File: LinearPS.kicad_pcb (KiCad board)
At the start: 2 copper layers, 100 x 100 mm, 84 parts, among them J1 Conn_01x03, J2 Conn_01x02, J3 Conn_01x03, J4 Conn_01x01, J5 Conn_01x01, J6 Conn_01x01, J7 Conn_01x01, J8 Conn_01x02, Q1 2N2222, Q2 TIP41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

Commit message: Added outputs for voltage and current meters
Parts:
- removed R28, R29: 10k, Resistors_THT:R_Axial_DIN0207_L6.3mm_D2.5mm_P7.62mm_Horizontal
- removed U3: LM7805_TO220, TO_SOT_Packages_THT:TO-220-3_Vertical
- added D22: 1N4733A, Diodes_THT:D_DO-41_SOD81_P7.62mm_Horizontal, F.Cu at (110.6, 53.4)
- added J9: Conn_01x02, Pin_Headers:Pin_Header_Straight_1x02_Pitch2.54mm, F.Cu at (104.7, 100.4)
- added R32: 1k, Resistors_THT:R_Axial_DIN0411_L9.9mm_D3.6mm_P12.70mm_Horizontal, F.Cu at (106.8, 65.8)
- added RV3: 10k, Potentiometers:Potentiometer_Trimmer_Bourns_3296W, F.Cu at (104.2, 95.7)
- added RV4: 10k, Potentiometers:Potentiometer_Trimmer_Bourns_3296W, F.Cu at (128.0, 100.2)
- added RV5: 10k, Potentiometers:Potentiometer_Trimmer_Bourns_3296W, F.Cu at (133.8, 97.9)
- moved J8 16.2 mm to (118.6, 64.5)
- moved R16 7.12 mm to (123.7, 110.0)
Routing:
- net Net-(D8-Pad1): track 80.8 -> 101.5 mm
- net Net-(C12-Pad1): track 17.6 -> 35.2 mm
- net Net-(C4-Pad1): track 156.4 -> 173.0 mm
- net GND: track 362.9 -> 353.0 mm
- net Net-(J3-Pad2): track 8.53 -> 17.9 mm
- net Net-(Q1-Pad2): track 45.1 -> 53.6 mm
- net Net-(R5-Pad1): track 7.37 -> 13.1 mm
- net Net-(Q2-Pad3): track 159.1 -> 153.8 mm
- net Net-(C1-Pad1): track 473.4 -> 477.4 mm
- net Net-(J3-Pad1): track 7.79 -> 10.5 mm
- net Net-(C6-Pad1): track 162.6 -> 164.3 mm
- net Net-(R23-Pad1): track 26.2 -> 27.1 mm
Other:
- board text removed: "LM7805"

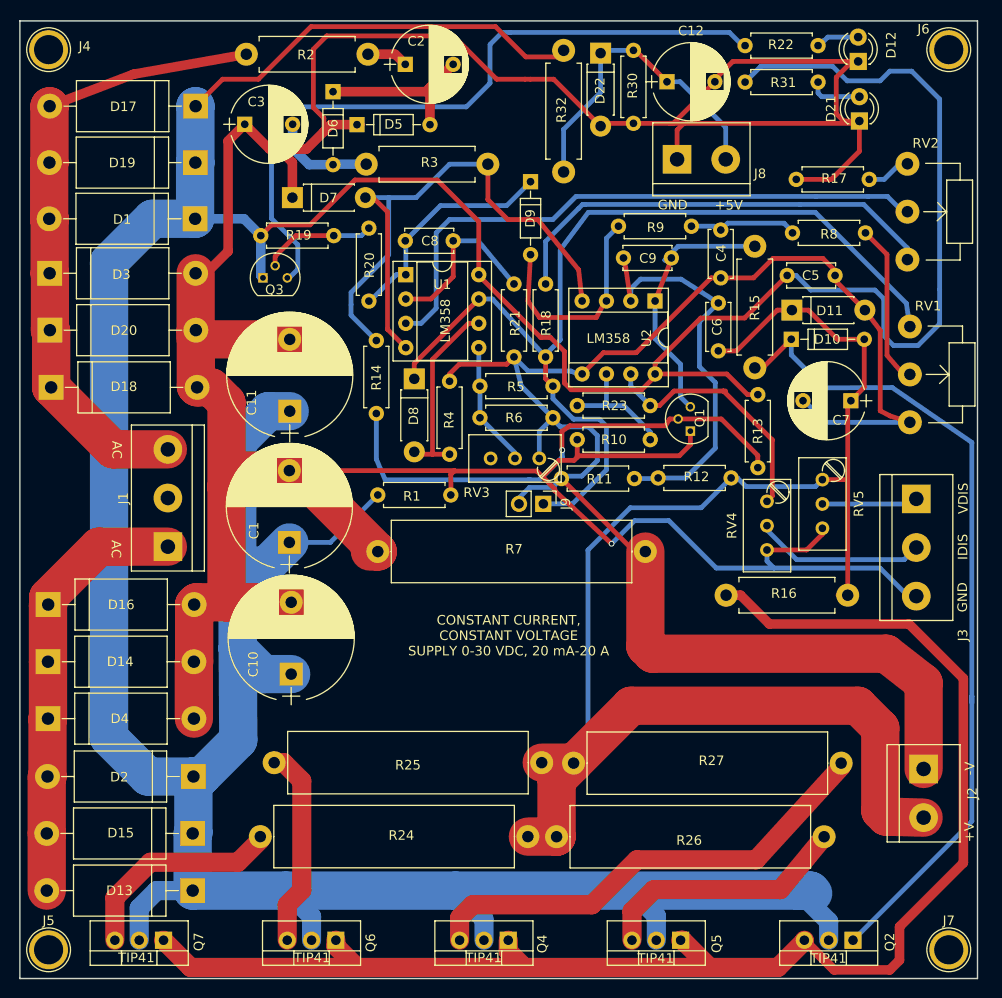
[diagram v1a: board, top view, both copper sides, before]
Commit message: Added better TO-220 mounting
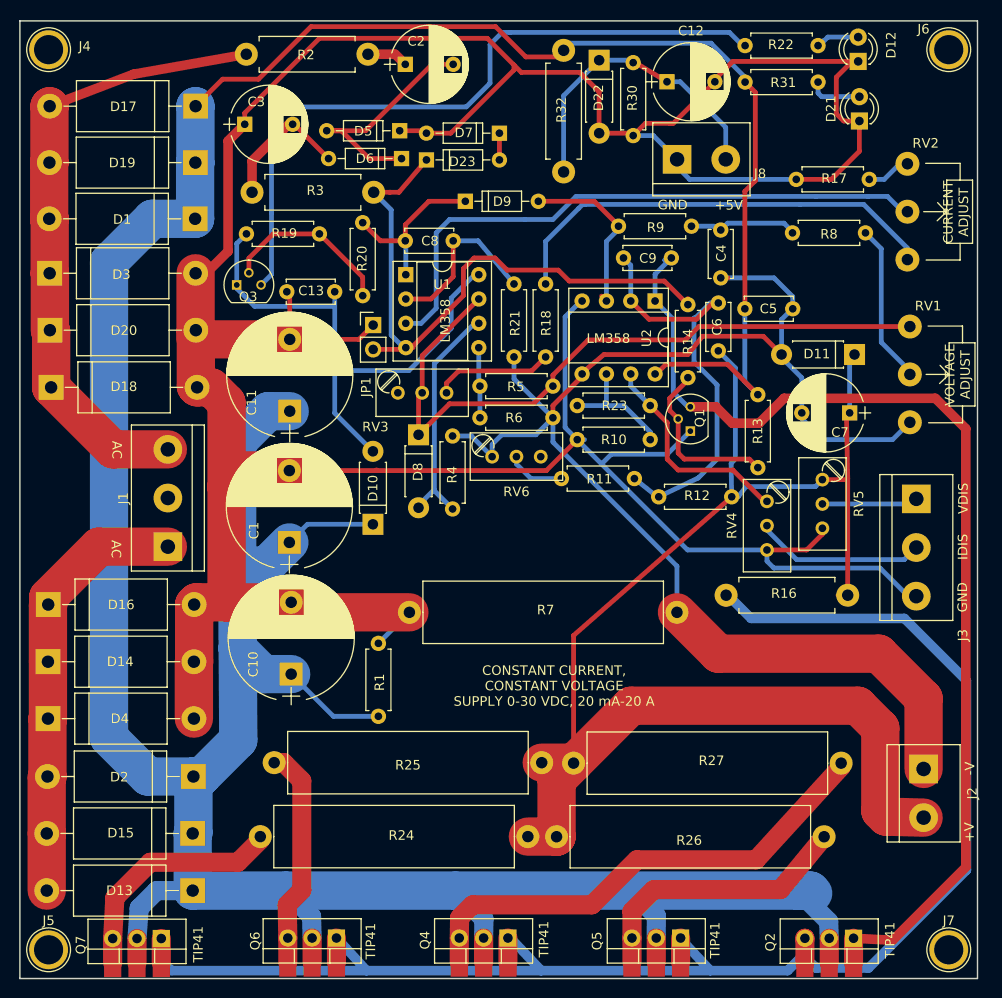
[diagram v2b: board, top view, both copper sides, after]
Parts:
- removed J9: Conn_01x02, Pin_Headers:Pin_Header_Straight_1x02_Pitch2.54mm
- removed R15: 1k, Resistors_THT:R_Axial_DIN0411_L9.9mm_D3.6mm_P12.70mm_Horizontal
- added C13: 100 nF, Capacitors_THT:C_Disc_D5.0mm_W2.5mm_P5.00mm, F.Cu at (77.9, 78.3)
- added D23: 1N4148, Diodes_THT:D_DO-35_SOD27_P7.62mm_Horizontal, F.Cu at (92.5, 64.5)
- added JP1: Jumper_NO_Small, Pin_Headers:Pin_Header_Straight_1x02_Pitch2.54mm, F.Cu at (86.9, 81.8)
- added RV6: 20k, Potentiometers:Potentiometer_Trimmer_Bourns_3296W, F.Cu at (99.3, 95.5)
- D10: value 1N4148 -> 1N4740A; footprint Diodes_THT:D_DO-35_SOD27_P7.62mm_Horizontal -> Diodes_THT:D_DO-41_SOD81_P7.62mm_Horizontal
- D7: value 1N5339B -> 1N4148; footprint Diodes_THT:D_DO-41_SOD81_P7.62mm_Horizontal -> Diodes_THT:D_DO-35_SOD27_P7.62mm_Horizontal
- Q2, Q4, Q5, Q6, Q7: footprint TO_SOT_Packages_THT:TO-220-3_Vertical -> linearps:TO-220-3_Vertical_WithPads
- R13: value 56k -> 22k
- R14: value 1k5 -> 1k
- R18: value 56k -> 33k
- RV3: value 10k -> 100k
- moved D10 47.8 mm to (86.9, 102.6), turned to 90 degrees
- moved R14 32.8 mm to (119.8, 79.6)
- moved R1 23.1 mm to (87.4, 122.6), turned to 90 degrees
- moved D7 22.6 mm to (100.1, 61.7), turned to 180 degrees
- moved RV3 16.3 mm to (89.5, 88.8), turned to 180 degrees
- moved R3 12.3 mm to (86.9, 67.9)
- moved D6 10.00 mm to (89.9, 64.4), turned to 180 degrees
- moved D11 8.02 mm to (137.2, 84.8), turned to 180 degrees
- moved R7 7.16 mm to (90.7, 111.8)
- moved D9 7.11 mm to (96.5, 68.8), turned to 0 degrees
- moved R20 7.08 mm to (85.8, 78.7), turned to 90 degrees
- moved D8 5.86 mm to (91.6, 93.2)
- moved R4 5.72 mm to (95.2, 101.0)
- moved C5 5.63 mm to (130.7, 80.1)
- moved D5 4.50 mm to (89.7, 61.5), turned to 180 degrees
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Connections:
- D10 pad 1: Net-(D10-Pad1) -> Net-(C1-Pad1)
- D10 pad 2: Net-(C6-Pad1) -> Net-(C13-Pad2)
- D7 pad 1: GND -> Net-(D23-Pad2)
- D7 pad 2: Net-(D7-Pad2) -> GND
- Q2 pad 1: Net-(D10-Pad1) -> Net-(C9-Pad1)
- Q3 pad 1: Net-(C1-Pad1) -> Net-(C13-Pad2)
- R11 pad 1: Net-(C4-Pad1) -> Net-(R11-Pad1)
- R14 pad 1: Net-(D7-Pad2) -> Net-(D23-Pad1)
- R18 pad 1: Net-(D8-Pad1) -> Net-(R18-Pad1)
- R19 pad 1: Net-(C1-Pad1) -> Net-(C13-Pad2)
- R3 pad 1: Net-(D7-Pad2) -> Net-(D23-Pad1)
- RV3 pad 1: Net-(C4-Pad1) -> (no net)
- RV3 pad 2: Net-(R5-Pad1) -> Net-(D8-Pad1)
- RV3 pad 3: (no net) -> Net-(R18-Pad1)
- U1 pad 4: Net-(D7-Pad2) -> Net-(D23-Pad1)
- U1 pad 8: Net-(C1-Pad1) -> Net-(C13-Pad2)
- U2 pad 4: Net-(D7-Pad2) -> GND
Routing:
- net Net-(C9-Pad1): track 28.6 -> 115.7 mm
- net Net-(D10-Pad1): track 86.6 -> 0.00 mm
- net Net-(C1-Pad1): track 477.4 -> 395.8 mm
- net Net-(D7-Pad2): track 70.0 -> 0.00 mm
- net Net-(D23-Pad1): track 0.00 -> 68.0 mm
- net Net-(C13-Pad2): track 0.00 -> 57.3 mm
- net Net-(Q1-Pad2): track 53.6 -> 18.0 mm, vias 1 -> 0
- net Net-(D8-Pad1): track 101.5 -> 74.2 mm
- net Net-(C4-Pad1): track 173.0 -> 152.4 mm
- net GND: track 353.0 -> 373.5 mm, vias 1 -> 0
- net Net-(Q2-Pad3): track 153.8 -> 172.0 mm
- net Net-(R18-Pad1): track 0.00 -> 12.8 mm
- net Net-(C6-Pad1): track 164.3 -> 155.4 mm
- net Net-(C2-Pad2): track 17.6 -> 25.1 mm
- net Net-(C8-Pad2): track 24.5 -> 17.9 mm
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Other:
- board text added: "CURRENT ADJUST"
- board text added: "VOLTAGE ADJUST"

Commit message: Change the voltage and current sense output
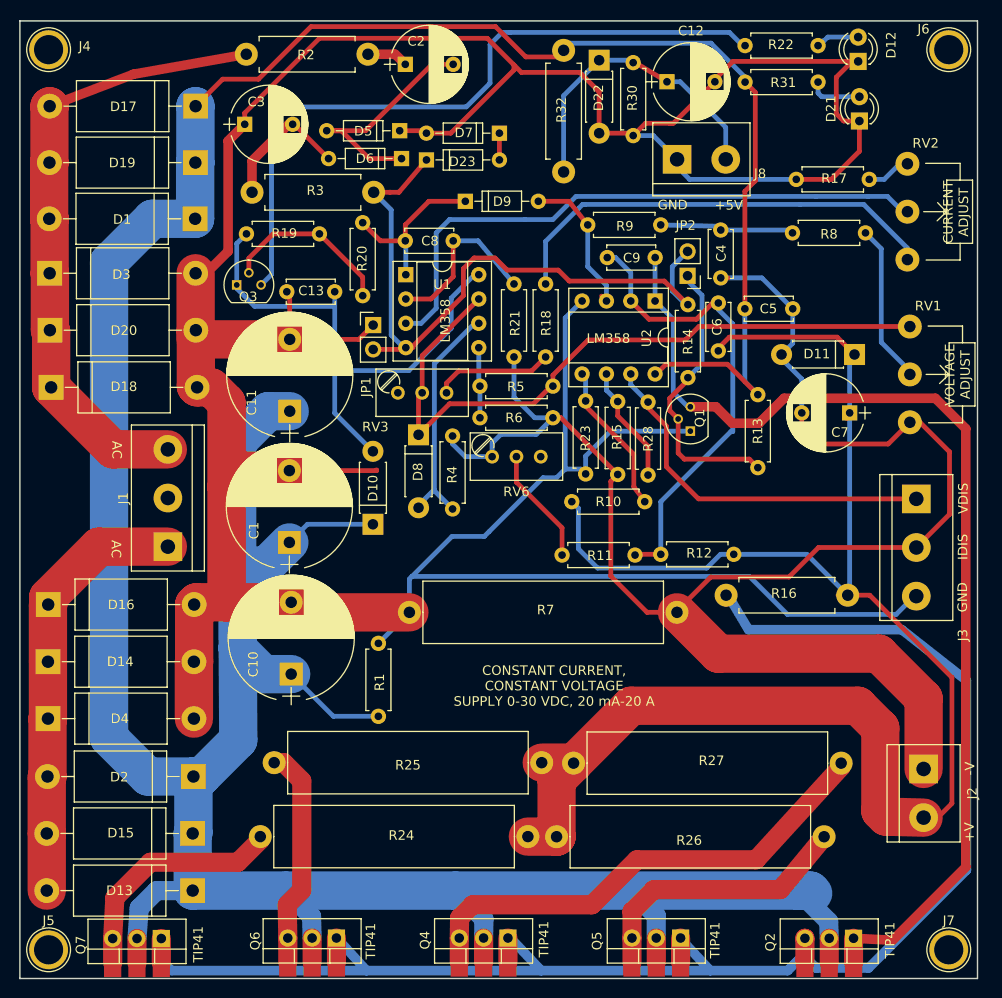
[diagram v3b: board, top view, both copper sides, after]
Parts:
- removed RV4, RV5: 10k, Potentiometers:Potentiometer_Trimmer_Bourns_3296W
- added JP2: Jumper_NO_Small, Pin_Headers:Pin_Header_Straight_1x02_Pitch2.54mm, F.Cu at (119.7, 76.6)
- added R15: 10k, Resistors_THT:R_Axial_DIN0207_L6.3mm_D2.5mm_P7.62mm_Horizontal, F.Cu at (112.4, 89.7)
- added R28: 10k, Resistors_THT:R_Axial_DIN0207_L6.3mm_D2.5mm_P7.62mm_Horizontal, F.Cu at (115.6, 89.8)
- R10: value 10k -> 100k
- moved R23 9.82 mm to (109.1, 97.3), turned to 90 degrees
- moved R11 7.99 mm to (106.6, 105.8)
- moved R10 6.50 mm to (107.6, 100.2)
- moved R12 6.01 mm to (124.5, 105.7)
- moved R9 3.21 mm to (109.3, 71.3)
- moved C9 1.69 mm to (116.3, 74.7)
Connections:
- J3 pad 2: Net-(J3-Pad2) -> Net-(C4-Pad1)
- R10 pad 1: GND -> Net-(C6-Pad1)
- R23 pad 1: Net-(R23-Pad1) -> GND
- U2 pad 5: Net-(C4-Pad1) -> Net-(R10-Pad2)
- U2 pad 6: Net-(R10-Pad2) -> Net-(R15-Pad1)
- U2 pad 7: Net-(R23-Pad1) -> Net-(J3-Pad1)
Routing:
- net Net-(J3-Pad1): track 10.5 -> 39.9 mm
- net Net-(R23-Pad1): track 23.3 -> 0.00 mm
- net Net-(C4-Pad1): track 152.4 -> 173.3 mm
- net Net-(C6-Pad1): track 155.4 -> 175.3 mm
- net Net-(J3-Pad2): track 17.9 -> 0.00 mm
- net GND: track 373.5 -> 388.7 mm
- net Net-(R15-Pad1): track 0.00 -> 12.8 mm
- net Net-(JP2-Pad1): track 18.0 -> 29.9 mm
- net Net-(D23-Pad1): track 68.0 -> 75.0 mm
- net Net-(R11-Pad1): track 6.45 -> 12.3 mm
- net Net-(C6-Pad2): track 45.0 -> 49.5 mm
- net Net-(R10-Pad2): track 13.5 -> 16.9 mm
- net Net-(C9-Pad1): track 115.7 -> 112.6 mm
- net Net-(C4-Pad2): track 11.5 -> 14.5 mm
- net Net-(D9-Pad2): track 19.1 -> 16.8 mm

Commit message: Changed voltage and current meter output
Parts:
- added JP3: Jumper_NO_Small, Pin_Headers:Pin_Header_Straight_1x02_Pitch2.54mm, F.Cu at (93.8, 105.9)
- Q1: value 2N2222 -> 2N3904
- Q3: value 2N2907 -> 2N3906
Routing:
- net GND: track 388.7 -> 370.7 mm
- net Net-(C13-Pad2): track 57.3 -> 74.4 mm
- net Net-(C1-Pad1): track 395.8 -> 404.6 mm
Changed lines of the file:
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@@
 (kicad_pcb (version 4) (host pcbnew 4.0.7)
   (general
-    (links 168)
+    (links 170)
     (no_connects 0)
     (area 49.924999 49.924999 150.075001 150.075001)
     (thickness 1.6)
     (drawings 23)
-    (tracks 608)
+    (tracks 612)
     (zones 0)
-    (modules 90)
+    (modules 91)
     (nets 42)
   )
@@
       (effects (font (size 1 1) (thickness 0.15)))
     )
-    (fp_text value 2N2222 (at 1.27 2.79 90) (layer F.Fab)
+    (fp_text value 2N3904 (at 1.27 2.79 90) (layer F.Fab)
       (effects (font (size 1 1) (thickness 0.15)))
     )
@@
       (effects (font (size 1 1) (thickness 0.15)))
     )
-    (fp_text value 2N2907 (at 1.27 2.79) (layer F.Fab)
+    (fp_text value 2N3906 (at 1.27 2.79) (layer F.Fab)
       (effects (font (size 1 1) (thickness 0.15)))
     )
@@
     )
   )
+  (module Pin_Headers:Pin_Header_Straight_1x02_Pitch2.54mm (layer F.Cu)
+    (at 93.76664 105.86466 90)
+    (descr "Through hole straight pin header, 1x02, 2.54mm pitch, single row")
+    (tags "Through hole pin header THT 1x02 2.54mm single row")
+    (fp_text reference JP3 (at 0.16764 5.588 90) (layer F.SilkS)
+      (effects (font (size 1 1) (thickness 0.15)))
+    )
+    (fp_text value Jumper_NO_Small (at 0 4.87 90) (layer F.Fab)
+      (effects (font (size 1 1) (thickness 0.15)))
+    )
+    (fp_line (start -0.635 -1.27) (end 1.27 -1.27) (layer F.Fab) (width 0.1))
+    (fp_line (start 1.27 -1.27) (end 1.27 3.81) (layer F.Fab) (width 0.1))
+    (fp_line (start 1.27 3.81) (end -1.27 3.81) (layer F.Fab) (width 0.1))
+    (fp_line (start -1.27 3.81) (end -1.27 -0.635) (layer F.Fab) (width 0.1))
+    (fp_line (start -1.27 -0.635) (end -0.635 -1.27) (layer F.Fab) (width 0.1))
+    (fp_line (start -1.33 3.87) (end 1.33 3.87) (layer F.SilkS) (width 0.12))
+    (fp_line (start -1.33 1.27) (end -1.33 3.87) (layer F.SilkS) (width 0.12))
+    (fp_line (start 1.33 1.27) (end 1.33 3.87) (layer F.SilkS) (width 0.12))
+    (fp_line (start -1.33 1.27) (end 1.33 1.27) (layer F.SilkS) (width 0.12))
+    (fp_line (start -1.33 0) (end -1.33 -1.33) (layer F.SilkS) (width 0.12))
+    (fp_line (start -1.33 -1.33) (end 0 -1.33) (layer F.SilkS) (width 0.12))
+    (fp_line (start -1.8 -1.8) (end -1.8 4.35) (layer F.CrtYd) (width 0.05))
+    (fp_line (start -1.8 4.35) (end 1.8 4.35) (layer F.CrtYd) (width 0.05))
+    (fp_line (start 1.8 4.35) (end 1.8 -1.8) (layer F.CrtYd) (width 0.05))
+    (fp_line (start 1.8 -1.8) (end -1.8 -1.8) (layer F.CrtYd) (width 0.05))
+    (fp_text user %R (at 0 1.27 180) (layer F.Fab)
+      (effects (font (size 1 1) (thickness 0.15)))
+    )
+    (pad 1 thru_hole rect (at 0 0 90) (size 1.7 1.7) (drill 1) (layers *.Cu *.Mask)
+      (net 1 "Net-(C1-Pad1)"))
+    (pad 2 thru_hole oval (at 0 2.54 90) (size 1.7 1.7) (drill 1) (layers *.Cu *.Mask)
+      (net 39 "Net-(C13-Pad2)"))
+    (model ${KISYS3DMOD}/Pin_Headers.3dshapes/Pin_Header_Straight_1x02_Pitch2.54mm.wrl
+      (at (xyz 0 0 0))
+      (scale (xyz 1 1 1))
+      (rotate (xyz 0 0 0))
+    )
+  )
   (gr_text "CURRENT\nADJUST" (at 147.7518 69.977 90) (layer F.SilkS)
     (effects (font (size 1 1) (thickness 0.15)))
@@
   (gr_line (start 150 50) (end 150 150) (angle 90) (layer Edge.Cuts) (width 0.15))
   (gr_line (start 50 50) (end 150 50) (angle 90) (layer Edge.Cuts) (width 0.15))
+  (segment (start 86.868 102.5652) (end 86.868 103.38054) (width 0.5) (layer B.Cu) (net 1) (status C00000))
+  (segment (start 86.868 103.38054) (end 89.35212 105.86466) (width 0.5) (layer B.Cu) (net 1) (status 400000))
+  (segment (start 89.35212 105.86466) (end 93.76664 105.86466) (width 0.5) (layer B.Cu) (net 1) (status 800000))
   (segment (start 134.5184 145.796) (end 134.5184 148.336) (width 2) (layer F.Cu) (net 1) (status 30))
   (segment (start 116.459 145.7706) (end 116.459 148.3106) (width 2) (layer F.Cu) (net 1) (status 30))
@@
   (segment (start 68.3006 64.8208) (end 68.326 64.7954) (width 4) (layer B.Cu) (net 1) (status 30))
   (segment (start 68.1228 134.7724) (end 68.0466 134.8486) (width 4) (layer B.Cu) (net 1) (status 30))
+  (segment (start 106.9467 96.7994) (end 106.9467 97.46234) (width 0.5) (layer B.Cu) (net 2))
+  (segment (start 105.34904 99.06) (end 105.34904 108.01604) (width 0.5) (layer B.Cu) (net 2))
+  (segment (start 106.9467 97.46234) (end 105.34904 99.06) (width 0.5) (layer B.Cu) (net 2))
   (segment (start 143.6116 110.0709) (end 143.41094 110.0709) (width 0.5) (layer B.Cu) (net 2))
   (segment (start 143.41094 110.0709) (end 141.5034 111.97844) (width 0.5) (layer B.Cu) (net 2))
-  (segment (start 126.19228 108.01604) (end 90.94216 108.01604) (width 0.5) (layer B.Cu) (net 2))
-  (segment (start 130.15468 111.97844) (end 126.19228 108.01604) (width 0.5) (layer B.Cu) (net 2))
   (segment (start 141.5034 111.97844) (end 130.15468 111.97844) (width 0.5) (layer B.Cu) (net 2))
+  (segment (start 130.15468 111.97844) (end 126.19228 108.01604) (width 0.5) (layer B.Cu) (net 2))
+  (segment (start 126.19228 108.01604) (end 105.34904 108.01604) (width 0.5) (layer B.Cu) (net 2))
+  (segment (start 105.34904 108.01604) (end 90.94216 108.01604) (width 0.5) (layer B.Cu) (net 2))
   (segment (start 109.08284 97.3074) (end 109.08284 95.43796) (width 0.5) (layer B.Cu) (net 2))
   (segment (start 111.6838 92.837) (end 120.015 92.837) (width 0.5) (layer B.Cu) (net 2))
@@
   (segment (start 106.9467 81.0133) (end 108.712 79.248) (width 0.5) (layer B.Cu) (net 2))
   (segment (start 106.9467 96.7994) (end 106.9467 81.0133) (width 0.5) (layer B.Cu) (net 2))
-  (segment (start 106.045 97.7011) (end 106.9467 96.7994) (width 0.5) (layer B.Cu) (net 2))
-  (segment (start 104.6353 97.7011) (end 106.045 97.7011) (width 0.5) (layer B.Cu) (net 2))
-  (segment (start 98.5012 103.8352) (end 98.9965 103.3399) (width 0.5) (layer B.Cu) (net 2))
-  (segment (start 98.9965 103.3399) (end 104.6353 97.7011) (width 0.5) (layer B.Cu) (net 2))
-  (segment (start 95.123 103.8352) (end 98.5012 103.8352) (width 0.5) (layer B.Cu) (net 2))
   (segment (start 90.678 108.2802) (end 90.94216 108.01604) (width 0.5) (layer B.Cu) (net 2))
-  (segment (start 90.94216 108.01604) (end 95.123 103.8352) (width 0.5) (layer B.Cu) (net 2))
   (segment (start 78.1812 83.2542) (end 85.4018 83.2542) (width 0.5) (layer F.Cu) (net 2))
   (segment (start 85.4018 83.2542) (end 86.8934 81.7626) (width 0.5) (layer F.Cu) (net 2))
@@
   (segment (start 78.1812 78.5876) (end 77.8764 78.2828) (width 0.5) (layer F.Cu) (net 2))
   (segment (start 87.4395 114.9985) (end 90.678 111.76) (width 0.5) (layer B.Cu) (net 2))
-  (segment (start 87.249 96.9575) (end 87.249 96.901) (width 0.5) (layer F.Cu) (net 2))
-  (segment (start 87.249 96.901) (end 87.249 96.9575) (width 0.5) (layer F.Cu) (net 2))
-  (segment (start 78.1431 96.9575) (end 87.249 96.9575) (width 0.5) (layer F.Cu) (net 2))
   (segment (start 90.678 111.76) (end 79.382 111.76) (width 4) (layer F.Cu) (net 2) (status 10))
   (segment (start 79.382 111.76) (end 78.3336 110.7116) (width 4) (layer F.Cu) (net 2))
@@
   (segment (start 94.5515 87.8205) (end 95.8215 86.5505) (width 0.5) (layer F.Cu) (net 38))
   (segment (start 104.902 85.09) (end 104.902 84.836) (width 0.5) (layer B.Cu) (net 38) (status 30))
+  (segment (start 86.868 94.9452) (end 86.868 96.0882) (width 0.5) (layer B.Cu) (net 39) (status 400000))
+  (segment (start 94.37878 103.9368) (end 96.30664 105.86466) (width 0.5) (layer B.Cu) (net 39) (status 800000))
+  (segment (start 90.5637 103.9368) (end 94.37878 103.9368) (width 0.5) (layer B.Cu) (net 39))
+  (segment (start 89.535 102.9081) (end 90.5637 103.9368) (width 0.5) (layer B.Cu) (net 39))
+  (segment (start 89.535 98.7552) (end 89.535 102.9081) (width 0.5) (layer B.Cu) (net 39))
+  (segment (start 86.868 96.0882) (end 89.535 98.7552) (width 0.5) (layer B.Cu) (net 39))
   (segment (start 72.644 77.5716) (end 72.644 77.9272) (width 0.5) (layer B.Cu) (net 39))
   (segment (start 72.644 77.9272) (end 74.5236 79.8068) (width 0.5) (layer B.Cu) (net 39))
